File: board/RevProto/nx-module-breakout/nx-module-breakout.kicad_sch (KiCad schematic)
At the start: 49 parts, among them J1 Conn_02x15_Odd_Even, J10 FTSH-105-01-L-DV-007-K, J2 DF40C-60DS-0.4V(51), J3 Conn_02x15_Odd_Even, J4 Conn_02x15_Odd_Even, J5 DF40C-60DS-0.4V(51), J6 SFV22R-2STE1HLF, J7 SFV22R-2STE1HLF, J8 Conn_02x06_Odd_Even, J9 USB_C_Receptacle_USB2.0_14P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

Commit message: Layout and routing for breakout JTAG connector
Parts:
- added JP6: SolderJumper_2_Bridged, Jumper:SolderJumper-2_P1.3mm_Bridged_RoundedPad1.0x1.5mm, symbol Jumper:SolderJumper_2_Bridged
- LOGO1: footprint CUSTOM:tinyAI_4_5mm -> CUSTOM:tinyAI_logo
- Q1: footprint Package_TO_SOT_SMD:SOT-23 -> Package_TO_SOT_SMD:SOT-323_SC-70
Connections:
- net JTAG_EN: now also RN4.3 (R3.1); no longer RN4.4 (R4.1)
- net PROGRAMn: now also JP6.2 (B); no longer J10.10 (Pin_10)
- net TDI: now also RN4.1 (R1.1); no longer RN4.3 (R3.1)
- net TMS: now also RN4.4 (R4.1); no longer RN4.1 (R1.1)
- new net: J10.10 (Pin_10), JP6.1 (A)
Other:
- moved on the sheet: R2

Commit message: Skew match remaining differential pairs of breakout
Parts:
- F1: value MF-FSMF035X-2 -> MF-FSMF050X-2
- renumbered JP5 to JP4, JP4 to JP5
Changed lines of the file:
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@@
 			)
 		)
-		(property "Value" "MF-FSMF035X-2"
+		(property "Value" "MF-FSMF050X-2"
 			(at 90.678 29.972 90)
 			(effects
@@
 		(on_board yes)
 		(dnp no)
-		(property "Reference" "JP5"
+		(property "Reference" "JP4"
 			(at 167.64 58.928 0)
 			(effects
@@
 			(project "nx-module-breakout"
 				(path "/c4309d17-8b44-40eb-9117-2333970d29f8"
-					(reference "JP5")
+					(reference "JP4")
 					(unit 1)
 				)
@@
 		(on_board yes)
 		(dnp no)
-		(property "Reference" "JP4"
+		(property "Reference" "JP5"
 			(at 167.64 66.548 0)
 			(effects
@@
 			(project "nx-module-breakout"
 				(path "/c4309d17-8b44-40eb-9117-2333970d29f8"
-					(reference "JP4")
+					(reference "JP5")
 					(unit 1)
 				)

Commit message: Remove pull-ups on breakout USB CC pins
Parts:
- removed R23, R24: 56K, Resistor_SMD:R_0402_1005Metric, symbol Device:R_Small
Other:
- moved on the sheet: R22, R25

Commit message: Add weak pull-up to breakout FPGA_EN
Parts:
- added JP7: SolderJumper_2_Bridged, Jumper:SolderJumper-2_P1.3mm_Bridged_RoundedPad1.0x1.5mm, symbol Jumper:SolderJumper_2_Bridged
- added R5: 56K, Resistor_SMD:R_0402_1005Metric, symbol Device:R_Small
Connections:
- net FPGA_EN: now also R5.2
- net P5VD_AON: now also JP7.2 (B)
- new net: JP7.1 (A), R5.1
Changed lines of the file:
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@@
 	(wire
 		(pts
+			(xy 261.62 80.01) (xy 261.62 73.66)
+		)
+		(stroke
+			(width 0)
+			(type default)
+		)
+	)
+	(wire
+		(pts
 			(xy 130.81 180.34) (xy 130.81 151.13)
 		)
@@
 	(wire
 		(pts
+			(xy 261.62 53.34) (xy 261.62 57.15)
+		)
+		(stroke
+			(width 0)
+			(type default)
+		)
+	)
+	(wire
+		(pts
 			(xy 279.4 135.89) (xy 269.24 135.89)
 		)
@@
 	(wire
 		(pts
+			(xy 261.62 64.77) (xy 261.62 68.58)
+		)
+		(stroke
+			(width 0)
+			(type default)
+		)
+	)
+	(wire
+		(pts
 			(xy 200.66 118.11) (xy 190.5 118.11)
 		)
@@
 		)
 	)
+	(label "FPGA_EN"
+		(at 261.62 80.01 270)
+		(effects
+			(font
+				(size 1.27 1.27)
+			)
+			(justify right bottom)
+		)
+	)
 	(label "MISO"
 		(at 240.03 82.55 270)
@@
 		)
 	)
+	(label "P5VD_AON"
+		(at 261.62 53.34 180)
+		(effects
+			(font
+				(size 1.27 1.27)
+			)
+			(justify right bottom)
+		)
+	)
 	(label "P3V3D"
 		(at 381 38.1 0)
@@
 	)
 	(symbol
+		(lib_id "Jumper:SolderJumper_2_Bridged")
+		(at 261.62 60.96 90)
+		(unit 1)
+		(exclude_from_sim no)
+		(in_bom no)
+		(on_board yes)
+		(dnp no)
+		(fields_autoplaced yes)
+		(property "Reference" "JP7"
+			(at 264.16 59.6899 90)
+			(effects
+				(font
+					(size 1.27 1.27)
+				)
+				(justify right)
+			)
+		)
+		(property "Value" "SolderJumper_2_Bridged"
+			(at 264.16 62.2299 90)
+			(effects
+				(font
+					(size 1.27 1.27)
+				)
+				(justify right)
+				(hide yes)
+			)
+		)
+		(property "Footprint" "Jumper:SolderJumper-2_P1.3mm_Bridged_RoundedPad1.0x1.5mm"
+			(at 261.62 60.96 0)
+			(effects
+				(font
+					(size 1.27 1.27)
+				)
+				(hide yes)
+			)
+		)
+		(property "Datasheet" "~"
+			(at 261.62 60.96 0)
+			(effects
+				(font
+					(size 1.27 1.27)
+				)
+				(hide yes)
+			)
+		)
+		(property "Description" "Solder Jumper, 2-pole, closed/bridged"
+			(at 261.62 60.96 0)
+			(effects
+				(font
+					(size 1.27 1.27)
+				)
+				(hide yes)
+			)
+		)
+		(pin "1"
+		)
+		(pin "2"
+		)
+		(instances
+			(project ""
+				(path "/c4309d17-8b44-40eb-9117-2333970d29f8"
+					(reference "JP7")
+					(unit 1)
+				)
+			)
+		)
+	)
+	(symbol
 		(lib_id "power:GND")
 		(at 269.24 168.91 90)
@@
 					(unit 1)
 				)
+			)
+		)
+	)
+	(symbol
+		(lib_id "Device:R_Small")
+		(at 261.62 71.12 0)
+		(unit 1)
+		(exclude_from_sim no)
+		(in_bom yes)
+		(on_board yes)
+		(dnp no)
+		(property "Reference" "R5"
+			(at 256.921 71.12 90)
+			(effects
+				(font
+					(size 1.27 1.27)
+				)
+			)
+		)
+		(property "Value" "56K"
+			(at 259.207 70.866 90)
+			(effects
+				(font
+					(size 1.27 1.27)
+				)
+			)
+		)
+		(property "Footprint" "Resistor_SMD:R_0402_1005Metric"
+			(at 261.62 71.12 0)
+			(effects
+				(font
+					(size 1.27 1.27)
+				)
+				(hide yes)
+			)
+		)
+		(property "Datasheet" "~"
+			(at 261.62 71.12 0)
+			(effects
+				(font
+					(size 1.27 1.27)
+				)
+				(hide yes)
+			)
+		)
+		(property "Description" "Resistor, small symbol"
+			(at 261.62 71.12 0)
+			(effects
+				(font
+					(size 1.27 1.27)
+				)
+				(hide yes)
+			)
+		)
+		(property "Digi-Key Part Number" ""
+			(at 261.62 71.12 0)
+			(effects
+				(font
+					(size 1.27 1.27)
+				)
+				(hide yes)
+			)
+		)
+		(property "MPN" "RC0402FR-0727RL"
+			(at 261.62 71.12 0)
+			(effects
+				(font
+					(size 1.27 1.27)
+				)
+				(hide yes)
+			)
+		)
+		(property "Manufacturer" "YAGEO"
+			(at 261.62 71.12 0)
+			(effects
+				(font
+					(size 1.27 1.27)
+				)
+				(hide yes)
+			)
+		)
+		(property "Supplier" "LCSC"
+			(at 261.62 71.12 0)
+			(effects
+				(font
+					(size 1.27 1.27)
+				)
+				(hide yes)
+			)
+		)
+		(pin "1"
+		)
+		(pin "2"
+		)
+		(instances
+			(project "nx-module-breakout"
+				(path "/c4309d17-8b44-40eb-9117-2333970d29f8"
+					(reference "R5")
+					(unit 1)
+				)

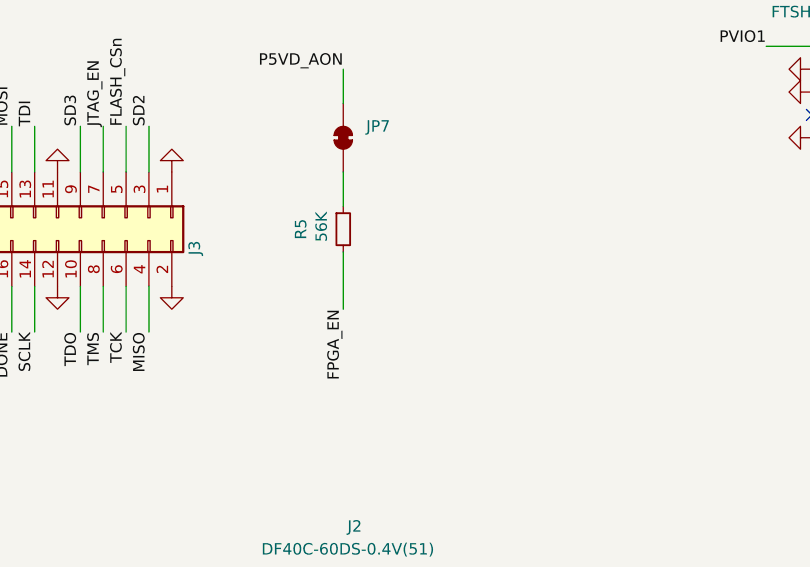
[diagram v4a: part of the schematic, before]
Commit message: Shutdown breakout regulators if module is fitted backwards
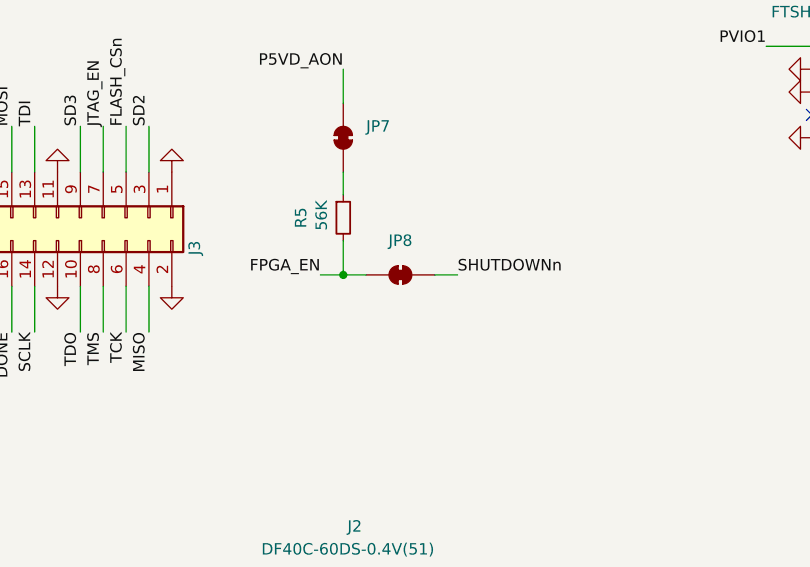
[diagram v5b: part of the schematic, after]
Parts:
- added JP8: SolderJumper_2_Bridged, Jumper:SolderJumper-2_P1.3mm_Bridged_RoundedPad1.0x1.5mm, symbol Jumper:SolderJumper_2_Bridged
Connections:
- net FPGA_EN: now also JP8.2 (B)
- net SHUTDOWNn: now also JP8.1 (A)
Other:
- moved on the sheet: R5
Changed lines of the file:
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@@
 	)
 	(junction
+		(at 261.62 76.2)
+		(diameter 0)
+		(color 0 0 0 0)
+	)
+	(junction
 		(at 113.03 177.8)
 		(diameter 0)
@@
 	(wire
 		(pts
-			(xy 261.62 80.01) (xy 261.62 73.66)
-		)
-		(stroke
-			(width 0)
-			(type default)
-		)
-	)
-	(wire
-		(pts
 			(xy 130.81 180.34) (xy 130.81 151.13)
 		)
@@
 	(wire
 		(pts
+			(xy 271.78 76.2) (xy 274.32 76.2)
+		)
+		(stroke
+			(width 0)
+			(type default)
+		)
+	)
+	(wire
+		(pts
 			(xy 55.88 163.83) (xy 58.42 163.83)
 		)
@@
 	(wire
 		(pts
-			(xy 261.62 64.77) (xy 261.62 68.58)
+			(xy 261.62 64.77) (xy 261.62 67.31)
 		)
 		(stroke
@@
 	(wire
 		(pts
+			(xy 261.62 76.2) (xy 264.16 76.2)
+		)
+		(stroke
+			(width 0)
+			(type default)
+		)
+	)
+	(wire
+		(pts
 			(xy 256.54 125.73) (xy 246.38 125.73)
 		)
@@
 	(wire
 		(pts
+			(xy 259.08 76.2) (xy 261.62 76.2)
+		)
+		(stroke
+			(width 0)
+			(type default)
+		)
+	)
+	(wire
+		(pts
 			(xy 109.22 107.95) (xy 146.05 107.95)
 		)
@@
 	(wire
 		(pts
+			(xy 261.62 76.2) (xy 261.62 72.39)
+		)
+		(stroke
+			(width 0)
+			(type default)
+		)
+	)
+	(wire
+		(pts
 			(xy 109.22 115.57) (xy 140.97 115.57)
 		)
@@
 	)
 	(label "FPGA_EN"
-		(at 261.62 80.01 270)
+		(at 259.08 76.2 180)
 		(effects
 			(font
@@
 		)
 	)
+	(label "SHUTDOWNn"
+		(at 274.32 76.2 0)
+		(effects
+			(font
+				(size 1.27 1.27)
+			)
+			(justify left bottom)
+		)
+	)
 	(label "PB22N"
 		(at 236.22 238.76 270)
@@
 	)
 	(symbol
+		(lib_id "Jumper:SolderJumper_2_Bridged")
+		(at 267.97 76.2 180)
+		(unit 1)
+		(exclude_from_sim no)
+		(in_bom no)
+		(on_board yes)
+		(dnp no)
+		(fields_autoplaced yes)
+		(property "Reference" "JP8"
+			(at 267.97 72.39 0)
+			(effects
+				(font
+					(size 1.27 1.27)
+				)
+			)
+		)
+		(property "Value" "SolderJumper_2_Bridged"
+			(at 269.2399 73.66 90)
+			(effects
+				(font
+					(size 1.27 1.27)
+				)
+				(justify right)
+				(hide yes)
+			)
+		)
+		(property "Footprint" "Jumper:SolderJumper-2_P1.3mm_Bridged_RoundedPad1.0x1.5mm"
+			(at 267.97 76.2 0)
+			(effects
+				(font
+					(size 1.27 1.27)
+				)
+				(hide yes)
+			)
+		)
+		(property "Datasheet" "~"
+			(at 267.97 76.2 0)
+			(effects
+				(font
+					(size 1.27 1.27)
+				)
+				(hide yes)
+			)
+		)
+		(property "Description" "Solder Jumper, 2-pole, closed/bridged"
+			(at 267.97 76.2 0)
+			(effects
+				(font
+					(size 1.27 1.27)
+				)
+				(hide yes)
+			)
+		)
+		(pin "1"
+		)
+		(pin "2"
+		)
+		(instances
+			(project "nx-module-breakout"
+				(path "/c4309d17-8b44-40eb-9117-2333970d29f8"
+					(reference "JP8")
+					(unit 1)
+				)
+			)
+		)
+	)
+	(symbol
 		(lib_id "Connector_Generic:Conn_02x15_Odd_Even")
 		(at 226.06 224.79 270)
@@
 	(symbol
 		(lib_id "Device:R_Small")
-		(at 261.62 71.12 0)
+		(at 261.62 69.85 0)
 		(unit 1)
 		(exclude_from_sim no)
@@
 		(dnp no)
 		(property "Reference" "R5"
-			(at 256.921 71.12 90)
+			(at 256.921 69.85 90)
 			(effects
 				(font
@@
 		)
 		(property "Value" "56K"
-			(at 259.207 70.866 90)
+			(at 259.207 69.596 90)
 			(effects
 				(font
@@
 		)
 		(property "Footprint" "Resistor_SMD:R_0402_1005Metric"
-			(at 261.62 71.12 0)
+			(at 261.62 69.85 0)
 			(effects
 				(font
@@
 		)
 		(property "Datasheet" "~"
-			(at 261.62 71.12 0)
+			(at 261.62 69.85 0)
 			(effects
 				(font
@@
 		)
 		(property "Description" "Resistor, small symbol"
-			(at 261.62 71.12 0)
+			(at 261.62 69.85 0)
 			(effects
 				(font
@@
 		)
 		(property "Digi-Key Part Number" ""
-			(at 261.62 71.12 0)
+			(at 261.62 69.85 0)
 			(effects
 				(font
@@
 		)
 		(property "MPN" "RC0402FR-0727RL"
-			(at 261.62 71.12 0)
+			(at 261.62 69.85 0)
 			(effects
 				(font
@@
 		)
 		(property "Manufacturer" "YAGEO"
-			(at 261.62 71.12 0)
+			(at 261.62 69.85 0)
 			(effects
 				(font
@@
 		)
 		(property "Supplier" "LCSC"
-			(at 261.62 71.12 0)
+			(at 261.62 69.85 0)
 			(effects
 				(font

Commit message: Misc breakout improvements
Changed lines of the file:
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@@
 		(dnp no)
 		(property "Reference" "R5"
-			(at 256.921 69.85 90)
+			(at 257.81 68.326 0)
 			(effects
 				(font
@@
 		)
 		(property "Value" "56K"
-			(at 259.207 69.596 90)
+			(at 258.064 70.612 0)
 			(effects
 				(font

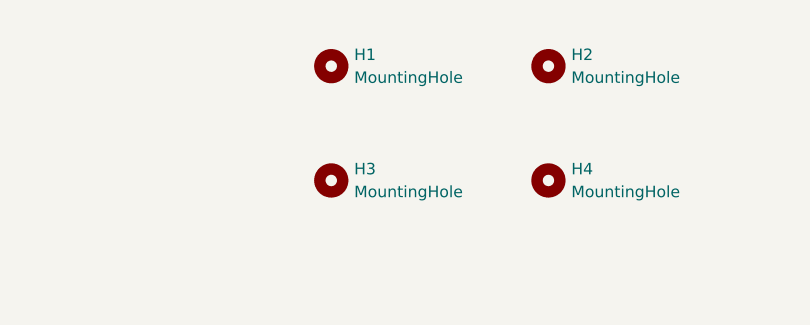
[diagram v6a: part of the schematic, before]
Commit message: Breakout: Add through hole pad for stand off
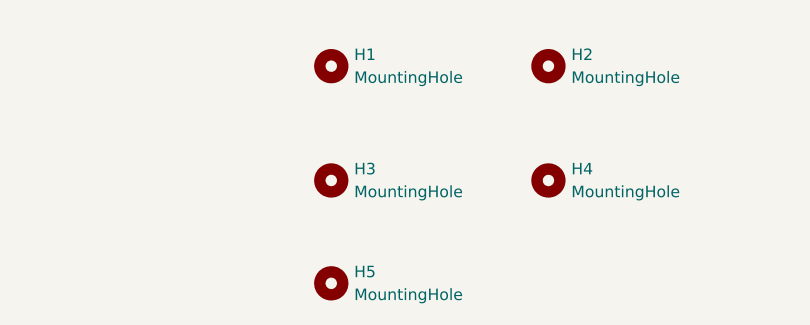
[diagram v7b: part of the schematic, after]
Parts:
- added H5: MountingHole, MountingHole:MountingHole_3mm_Pad, symbol Mechanical:MountingHole
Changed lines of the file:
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@@
+	)
+	(symbol
+		(lib_id "Mechanical:MountingHole")
+		(at 130.81 276.86 0)
+		(unit 1)
+		(exclude_from_sim no)
+		(in_bom no)
+		(on_board yes)
+		(dnp no)
+		(fields_autoplaced yes)
+		(property "Reference" "H5"
+			(at 133.35 275.5899 0)
+			(effects
+				(font
+					(size 1.27 1.27)
+				)
+				(justify left)
+			)
+		)
+		(property "Value" "MountingHole"
+			(at 133.35 278.1299 0)
+			(effects
+				(font
+					(size 1.27 1.27)
+				)
+				(justify left)
+			)
+		)
+		(property "Footprint" "MountingHole:MountingHole_3mm_Pad"
+			(at 130.81 276.86 0)
+			(effects
+				(font
+					(size 1.27 1.27)
+				)
+				(hide yes)
+			)
+		)
+		(property "Datasheet" "~"
+			(at 130.81 276.86 0)
+			(effects
+				(font
+					(size 1.27 1.27)
+				)
+				(hide yes)
+			)
+		)
+		(property "Description" "Mounting Hole without connection"
+			(at 130.81 276.86 0)
+			(effects
+				(font
+					(size 1.27 1.27)
+				)
+				(hide yes)
+			)
+		)
+		(instances
+			(project ""
+				(path "/c4309d17-8b44-40eb-9117-2333970d29f8"
+					(reference "H5")
+					(unit 1)
+				)
+			)
+		)
 	)
 	(symbol

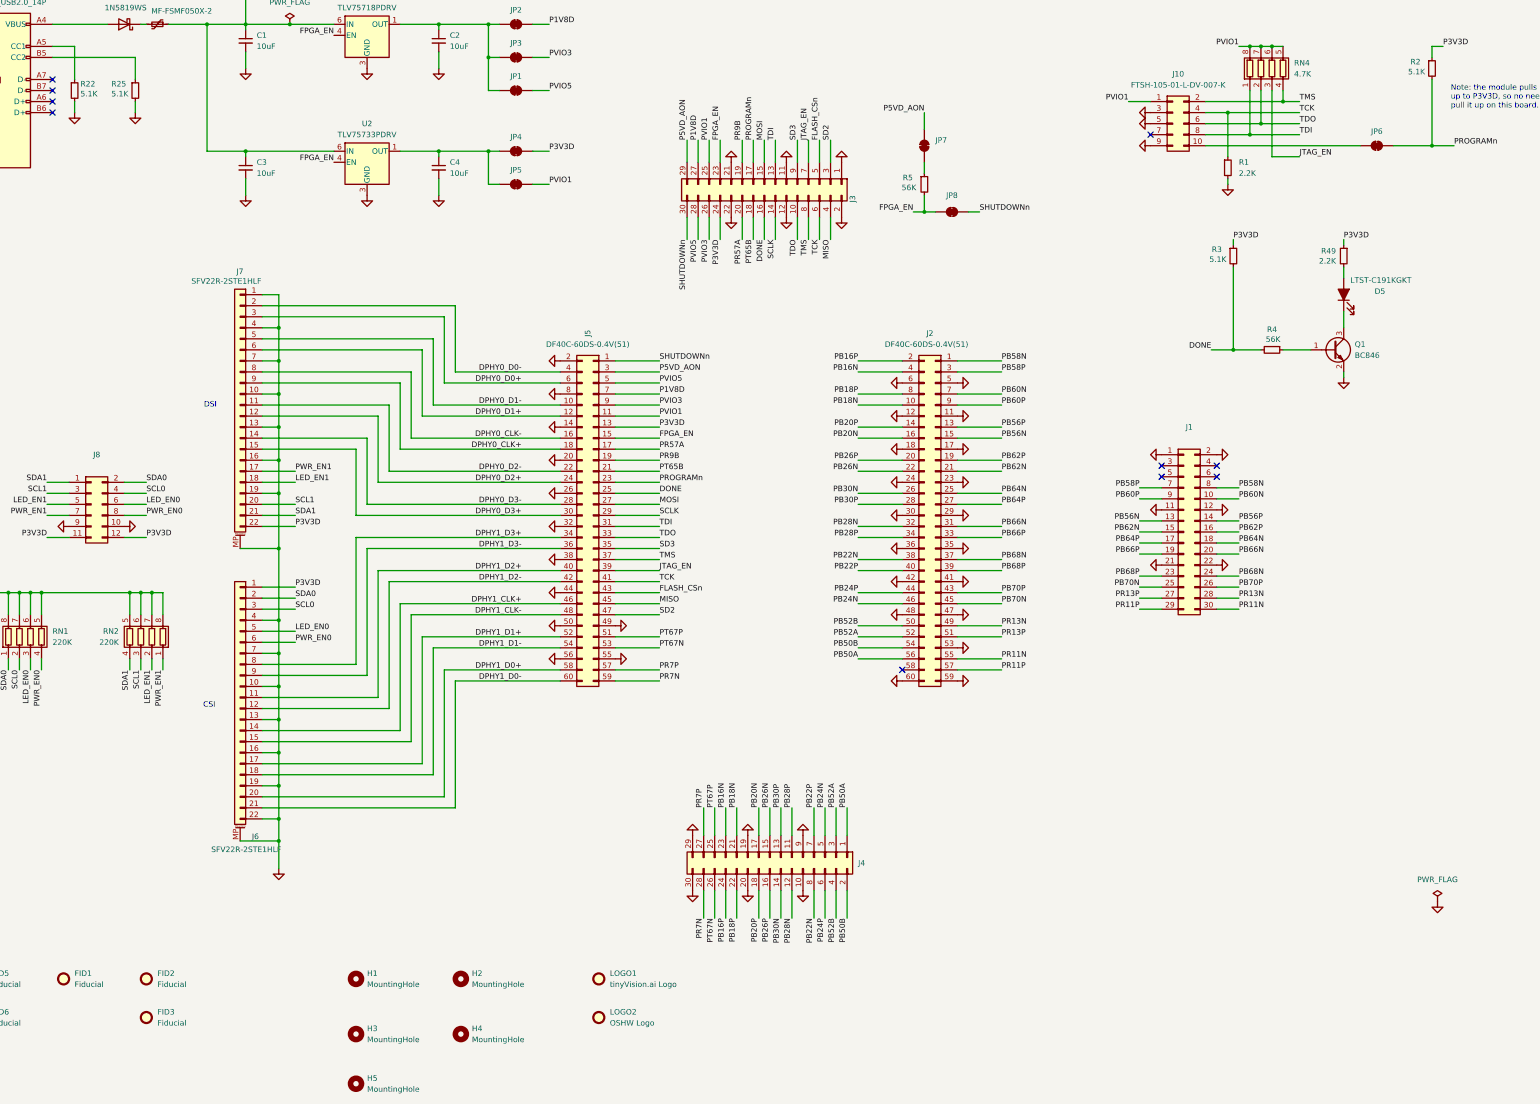
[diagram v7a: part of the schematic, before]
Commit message: Breakout: added 24MHz oscillator
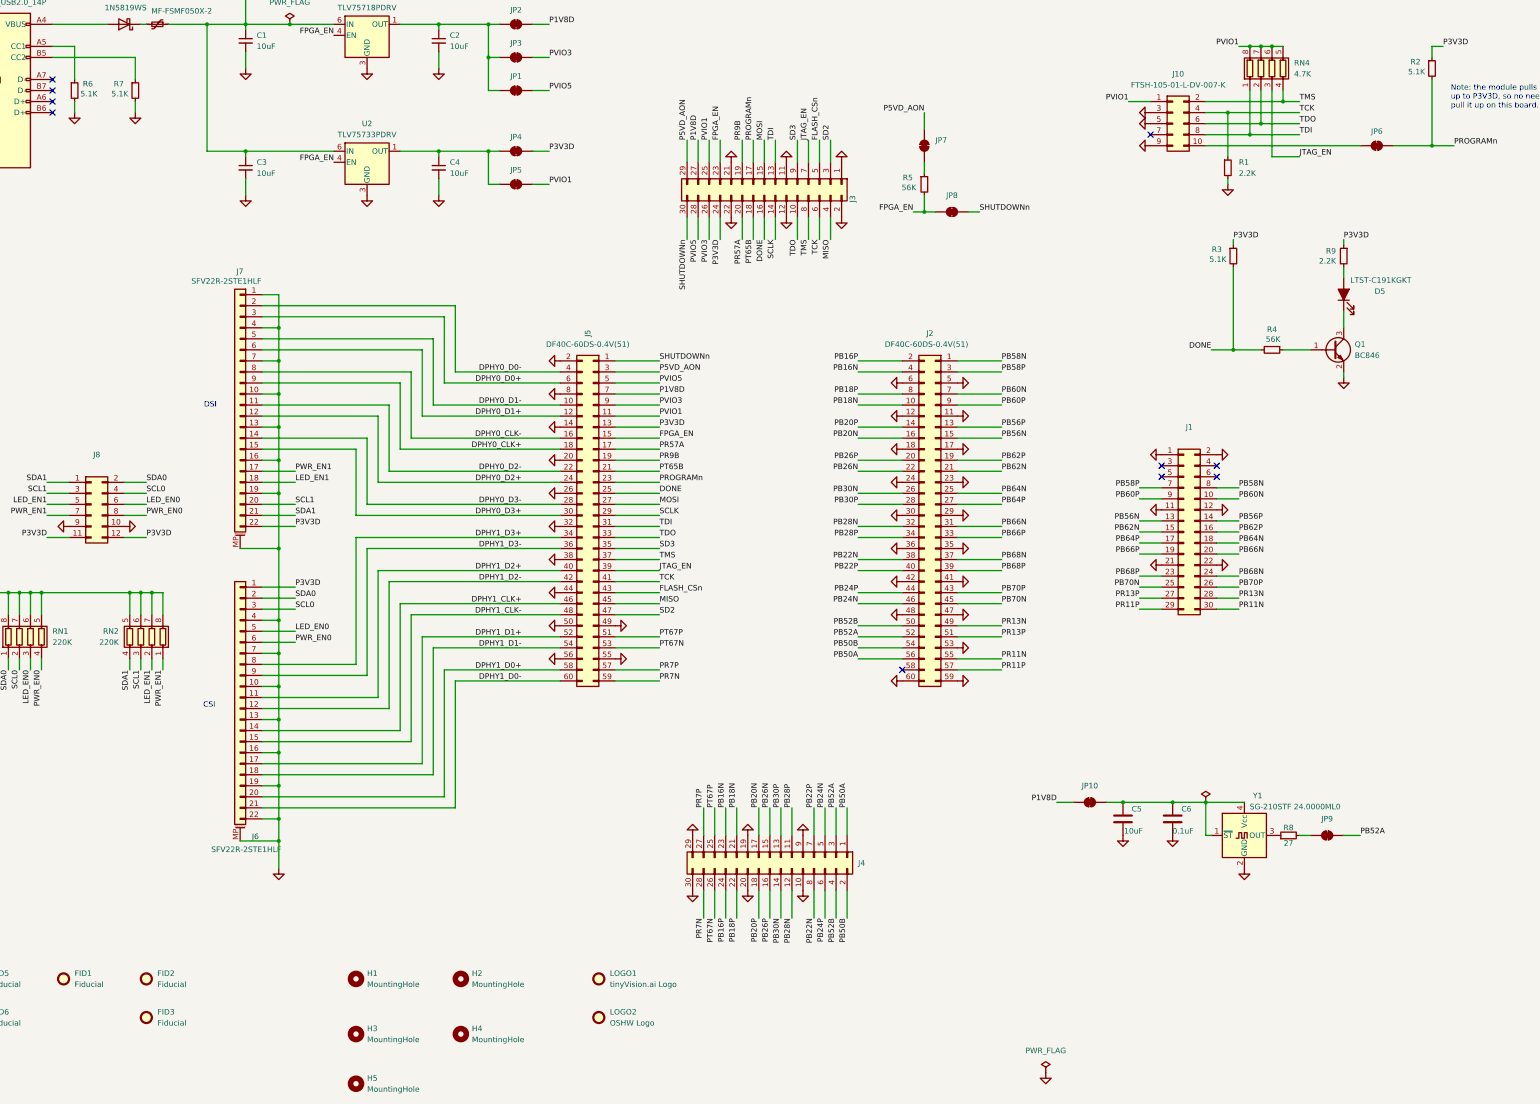
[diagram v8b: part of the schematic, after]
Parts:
- added C5: 10uF, Capacitor_SMD:C_0402_1005Metric, symbol Device:C
- added C6: 0.1uF, Capacitor_SMD:C_0201_0603Metric, symbol Device:C
- added JP10, JP9: SolderJumper_2_Bridged, Jumper:SolderJumper-2_P1.3mm_Bridged_RoundedPad1.0x1.5mm, symbol Jumper:SolderJumper_2_Bridged
- added R8: 27, Resistor_SMD:R_0402_1005Metric, symbol Device:R_Small
- added Y1: SG-210STF 24.0000ML0, Oscillator:Oscillator_SMD_SeikoEpson_SG210-4Pin_2.5x2.0mm, symbol Oscillator:SG-210STF
- renumbered R22 to R6, R25 to R7, R49 to R9
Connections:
- net GND: now also C5.1, C6.1, Y1.2 (GND)
- net P1V8D: now also JP10.2 (B)
- net PB52A: now also JP9.1 (A)
- new net: JP9.2 (B), R8.2
- new net: C5.2, C6.2, JP10.1 (A), Y1.1 (~{ST}), Y1.4 (Vcc)
- new net: R8.1, Y1.3 (OUT)
